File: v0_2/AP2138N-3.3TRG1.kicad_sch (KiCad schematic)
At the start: 9 parts, among them IC3 AP2138N-3.3TRG1, J1 S2B-PH-SM4-TB_LF__SN_, Q1 DMG2301L-7, Q2 DMG2301L-7, Q4 DMN3731U-13

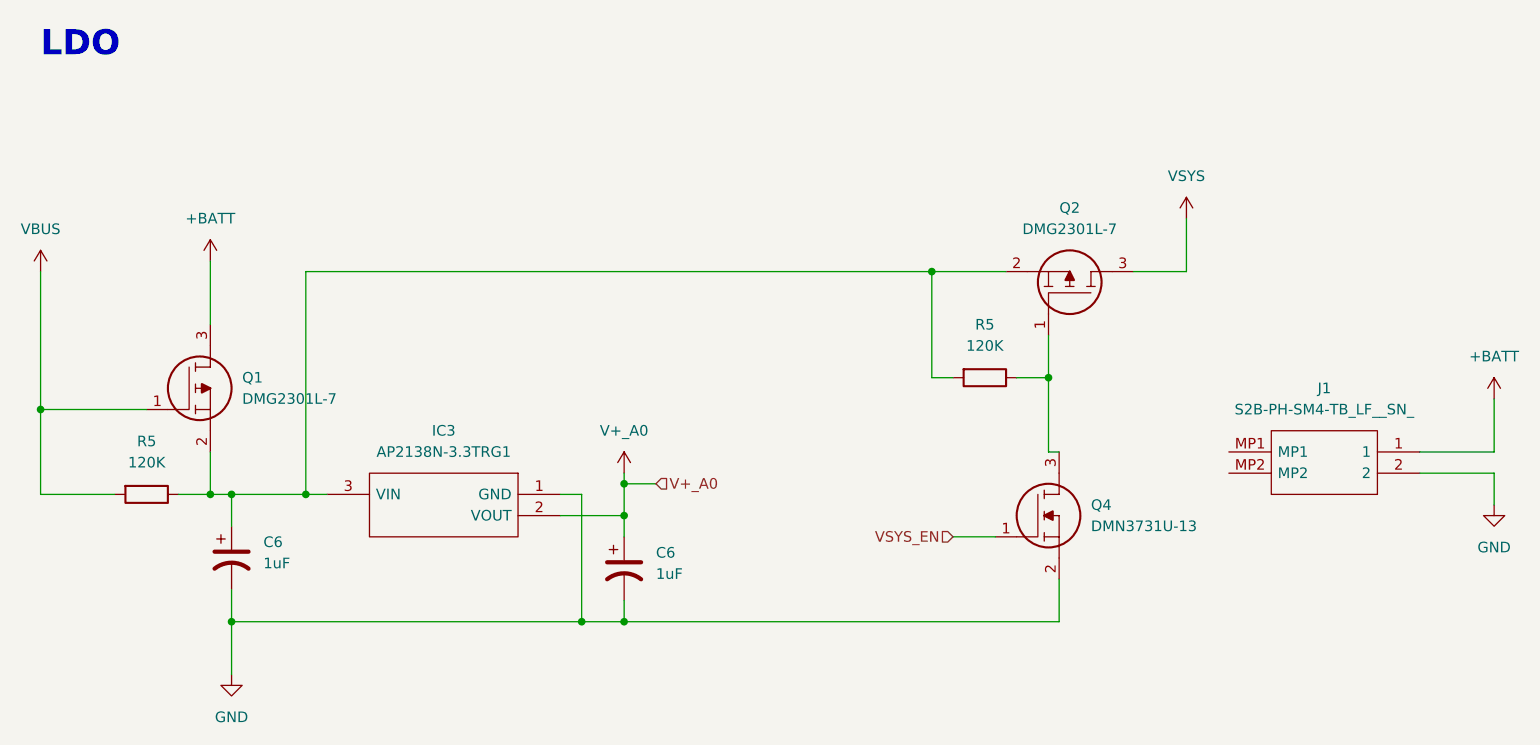
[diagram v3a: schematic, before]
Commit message: rename i2c and add button
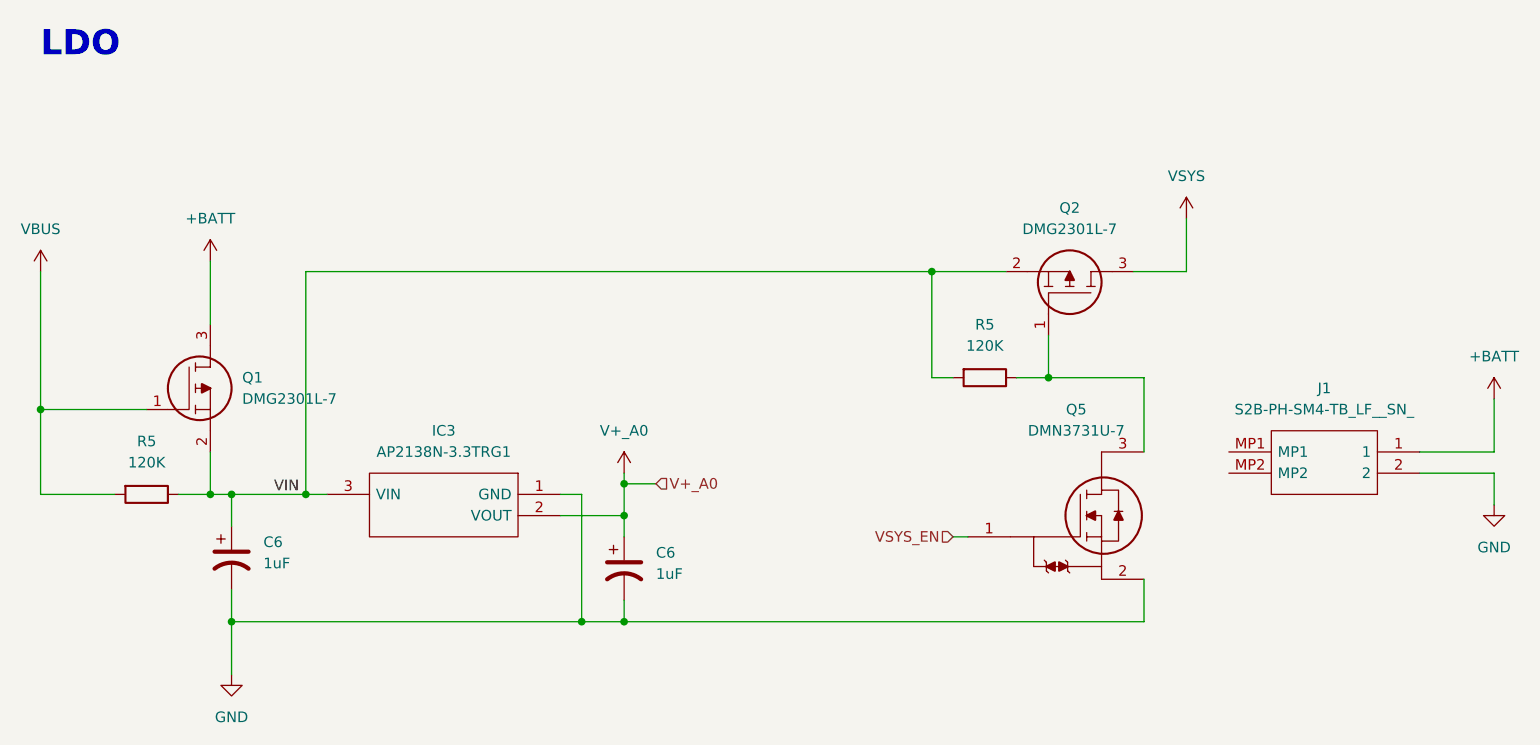
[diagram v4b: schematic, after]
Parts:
- removed Q4: DMN3731U-13, DMN3731U-13:SOT96P240X110-3N, symbol DMN3731U-13:DMN3731U-13
- added Q5: DMN3731U-7, DMN3731U-7:SOT96P240X110-3N, symbol DMN3731U-7:DMN3731U-7
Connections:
- net GND: now also Q5.2
- net VSYS_EN: now also Q5.1
- net at Q2.1, R5.1: now also Q5.3
- net VIN: now reaches C6.1, IC3.3 (VIN), Q1.2, Q2.2, R5.1, R5.2
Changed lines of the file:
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@@
   (junction (at 99.06 90.17) (diameter 0) (color 0 0 0 0)
   )
+  (junction (at 185.42 63.5) (diameter 0) (color 0 0 0 0)
+  )
+  (junction (at 110.49 90.17) (diameter 0) (color 0 0 0 0)
+  )
+  (junction (at 148.59 88.9) (diameter 0) (color 0 0 0 0)
+  )
+  (junction (at 78.74 80.01) (diameter 0) (color 0 0 0 0)
+  )
   (junction (at 199.39 76.2) (diameter 0) (color 0 0 0 0)
   )
-  (junction (at 185.42 63.5) (diameter 0) (color 0 0 0 0)
-  )
-  (junction (at 110.49 90.17) (diameter 0) (color 0 0 0 0)
-  )
-  (junction (at 148.59 88.9) (diameter 0) (color 0 0 0 0)
-  )
-  (junction (at 78.74 80.01) (diameter 0) (color 0 0 0 0)
+  (wire (pts (xy 210.82 76.2) (xy 199.39 76.2))
+    (stroke (width 0) (type default))
   )
   (wire (pts (xy 99.06 62.23) (xy 99.06 69.85))
@@
     (stroke (width 0) (type default))
   )
-  (wire (pts (xy 148.59 105.41) (xy 200.66 105.41))
+  (wire (pts (xy 148.59 105.41) (xy 210.82 105.41))
     (stroke (width 0) (type default))
   )
@@
     (stroke (width 0) (type default))
   )
-  (wire (pts (xy 187.96 95.25) (xy 193.04 95.25))
+  (wire (pts (xy 187.96 95.25) (xy 189.738 95.25))
     (stroke (width 0) (type default))
   )
@@
     (stroke (width 0) (type default))
   )
-  (wire (pts (xy 199.39 85.09) (xy 199.39 76.2))
-    (stroke (width 0) (type default))
-  )
   (wire (pts (xy 148.59 88.9) (xy 152.4 88.9))
     (stroke (width 0) (type default))
@@
     (stroke (width 0) (type default))
   )
+  (wire (pts (xy 210.82 85.09) (xy 210.82 76.2))
+    (stroke (width 0) (type default))
+  )
   (wire (pts (xy 199.39 71.12) (xy 199.39 76.2))
     (stroke (width 0) (type default))
@@
     (stroke (width 0) (type default))
   )
-  (wire (pts (xy 200.66 85.09) (xy 199.39 85.09))
+  (wire (pts (xy 210.82 100.33) (xy 210.82 105.41))
     (stroke (width 0) (type default))
   )
@@
   )
   (wire (pts (xy 101.6 105.41) (xy 101.6 111.76))
-    (stroke (width 0) (type default))
-  )
-  (wire (pts (xy 200.66 100.33) (xy 200.66 105.41))
     (stroke (width 0) (type default))
   )
@@
   (text "LDO" (at 78.74 38.1 0)
     (effects (font (face "Ubuntu") (size 3 3) (thickness 1) bold) (justify left bottom))
+  )
+  (label "VIN" (at 106.68 90.17 0) (fields_autoplaced)
+    (effects (font (size 1.27 1.27)) (justify left bottom))
   )
   (hierarchical_label "VSYS_EN" (shape input) (at 187.96 95.25 180) (fields_autoplaced)
@@
     )
   )
-  (symbol (lib_id "DMN3731U-13:DMN3731U-13") (at 193.04 95.25 0) (unit 1)
-    (in_bom yes) (on_board yes) (dnp no) (fields_autoplaced)
-    (property "Reference" "Q4" (at 204.47 91.44 0)
-      (effects (font (size 1.27 1.27)) (justify left))
-    )
-    (property "Value" "DMN3731U-13" (at 204.47 93.98 0)
-      (effects (font (size 1.27 1.27)) (justify left))
-    )
-    (property "Footprint" "DMN3731U-13:SOT96P240X110-3N" (at 204.47 96.52 0)
-      (effects (font (size 1.27 1.27)) (justify left) hide)
-    )
-    (property "Datasheet" "https://www.diodes.com/assets/Datasheets/DMN3731U.pdf" (at 204.47 99.06 0)
-      (effects (font (size 1.27 1.27)) (justify left) hide)
-    )
-    (property "Description" "MOSFET MOSFET BVDSS: 25V-30V" (at 204.47 101.6 0)
-      (effects (font (size 1.27 1.27)) (justify left) hide)
-    )
-    (property "Height" "1.1" (at 204.47 104.14 0)
-      (effects (font (size 1.27 1.27)) (justify left) hide)
-    )
-    (property "Manufacturer_Name" "Diodes Inc." (at 204.47 106.68 0)
-      (effects (font (size 1.27 1.27)) (justify left) hide)
-    )
-    (property "Manufacturer_Part_Number" "DMN3731U-13" (at 204.47 109.22 0)
-      (effects (font (size 1.27 1.27)) (justify left) hide)
-    )
-    (property "Mouser Part Number" "621-DMN3731U-13" (at 204.47 111.76 0)
-      (effects (font (size 1.27 1.27)) (justify left) hide)
-    )
-    (property "Mouser Price/Stock" "https://www.mouser.co.uk/ProductDetail/Diodes-Incorporated/DMN3731U-13?qs=EBDBlbfErPwOKX9Ga5s0uA%3D%3D" (at 204.47 114.3 0)
-      (effects (font (size 1.27 1.27)) (justify left) hide)
-    )
-    (property "Arrow Part Number" "" (at 204.47 116.84 0)
-      (effects (font (size 1.27 1.27)) (justify left) hide)
-    )
-    (property "Arrow Price/Stock" "" (at 204.47 119.38 0)
-      (effects (font (size 1.27 1.27)) (justify left) hide)
-    )
-    (pin "1")
-    (pin "2")
-    (pin "3")
-    (instances
-      (project "v0_2"
-        (path "/678523e5-508b-4706-b0e0-f17e466a8d09/3580e7c3-86d9-4e19-aad4-f7334a732566"
-          (reference "Q4") (unit 1)
-        )
-      )
-    )
-  )
   (symbol (lib_id "Device:R") (at 91.44 90.17 270) (unit 1)
     (in_bom yes) (on_board yes) (dnp no) (fields_autoplaced)
@@
         )
       )
+    )
+  )
+  (symbol (lib_id "DMN3731U-7:DMN3731U-7") (at 198.12 95.25 0) (unit 1)
+    (in_bom yes) (on_board yes) (dnp no) (fields_autoplaced)
+    (property "Reference" "Q5" (at 202.7174 80.01 0)
+      (effects (font (size 1.27 1.27)))
+    )
+    (property "Value" "DMN3731U-7" (at 202.7174 82.55 0)
+      (effects (font (size 1.27 1.27)))
+    )
+    (property "Footprint" "DMN3731U-7:SOT96P240X110-3N" (at 212.852 76.2 0)
+      (effects (font (size 1.27 1.27)) (justify left) hide)
+    )
+    (property "Datasheet" "https://www.mouser.fr/datasheet/2/115/DMN3731U-1594715.pdf" (at 212.852 78.74 0)
+      (effects (font (size 1.27 1.27)) (justify left) hide)
+    )
+    (property "Description" "MOSFET MOSFET BVDSS: 25V-30V" (at 212.852 81.28 0)
+      (effects (font (size 1.27 1.27)) (justify left) hide)
+    )
+    (property "Height" "1.1" (at 212.852 83.82 0)
+      (effects (font (size 1.27 1.27)) (justify left) hide)
+    )
+    (property "Manufacturer_Name" "Diodes Inc." (at 212.852 86.36 0)
+      (effects (font (size 1.27 1.27)) (justify left) hide)
+    )
+    (property "Manufacturer_Part_Number" "DMN3731U-7" (at 212.852 88.9 0)
+      (effects (font (size 1.27 1.27)) (justify left) hide)
+    )
+    (property "Mouser Part Number" "621-DMN3731U-7" (at 212.852 91.44 0)
+      (effects (font (size 1.27 1.27)) (justify left) hide)
+    )
+    (property "Mouser Price/Stock" "https://www.mouser.co.uk/ProductDetail/Diodes-Incorporated/DMN3731U-7?qs=EBDBlbfErPyEqvOCBrONHQ%3D%3D" (at 212.852 93.98 0)
+      (effects (font (size 1.27 1.27)) (justify left) hide)
+    )
+    (property "Arrow Part Number" "" (at 212.852 96.52 0)
+      (effects (font (size 1.27 1.27)) (justify left) hide)
+    )
+    (property "Arrow Price/Stock" "" (at 212.852 99.06 0)
+      (effects (font (size 1.27 1.27)) (justify left) hide)
+    )
+    (pin "1")
+    (pin "2")
+    (pin "3")
+    (instances
+      (project "v0_2"
+        (path "/678523e5-508b-4706-b0e0-f17e466a8d09/3580e7c3-86d9-4e19-aad4-f7334a732566"
+          (reference "Q5") (unit 1)
+        )
+      )

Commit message: power line
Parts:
- added J6: Conn_01x02_Pin, Connector_PinHeader_1.27mm:PinHeader_1x02_P1.27mm_Vertical, symbol Connector:Conn_01x02_Pin
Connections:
- net +BATT: now also J6.1 (Pin_1)
- net GND: now also J6.2 (Pin_2)
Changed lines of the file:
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@@
   (junction (at 101.6 105.41) (diameter 0) (color 0 0 0 0)
   )
+  (junction (at 247.65 85.09) (diameter 0) (color 0 0 0 0)
+  )
   (junction (at 148.59 105.41) (diameter 0) (color 0 0 0 0)
   )
@@
   (junction (at 199.39 76.2) (diameter 0) (color 0 0 0 0)
   )
+  (junction (at 250.19 87.63) (diameter 0) (color 0 0 0 0)
+  )
   (wire (pts (xy 210.82 76.2) (xy 199.39 76.2))
     (stroke (width 0) (type default))
@@
     (stroke (width 0) (type default))
   )
+  (wire (pts (xy 243.84 99.06) (xy 250.19 99.06))
+    (stroke (width 0) (type default))
+  )
   (wire (pts (xy 78.74 80.01) (xy 78.74 90.17))
     (stroke (width 0) (type default))
@@
     (stroke (width 0) (type default))
   )
-  (wire (pts (xy 243.84 85.09) (xy 252.73 85.09))
+  (wire (pts (xy 243.84 85.09) (xy 247.65 85.09))
     (stroke (width 0) (type default))
   )
@@
     (stroke (width 0) (type default))
   )
-  (wire (pts (xy 243.84 87.63) (xy 252.73 87.63))
+  (wire (pts (xy 243.84 87.63) (xy 250.19 87.63))
     (stroke (width 0) (type default))
   )
@@
     (stroke (width 0) (type default))
   )
-  (wire (pts (xy 187.96 95.25) (xy 189.738 95.25))
+  (wire (pts (xy 184.15 95.25) (xy 189.738 95.25))
     (stroke (width 0) (type default))
   )
@@
     (stroke (width 0) (type default))
   )
+  (wire (pts (xy 247.65 85.09) (xy 252.73 85.09))
+    (stroke (width 0) (type default))
+  )
   (wire (pts (xy 185.42 76.2) (xy 185.42 63.5))
     (stroke (width 0) (type default))
   )
+  (wire (pts (xy 250.19 87.63) (xy 252.73 87.63))
+    (stroke (width 0) (type default))
+  )
   (wire (pts (xy 99.06 85.09) (xy 99.06 90.17))
     (stroke (width 0) (type default))
@@
     (stroke (width 0) (type default))
   )
+  (wire (pts (xy 250.19 99.06) (xy 250.19 87.63))
+    (stroke (width 0) (type default))
+  )
+  (wire (pts (xy 247.65 96.52) (xy 247.65 85.09))
+    (stroke (width 0) (type default))
+  )
   (wire (pts (xy 101.6 90.17) (xy 110.49 90.17))
     (stroke (width 0) (type default))
@@
   )
   (wire (pts (xy 101.6 105.41) (xy 101.6 111.76))
+    (stroke (width 0) (type default))
+  )
+  (wire (pts (xy 243.84 96.52) (xy 247.65 96.52))
     (stroke (width 0) (type default))
   )
@@
     (effects (font (size 1.27 1.27)) (justify left bottom))
   )
-  (hierarchical_label "VSYS_EN" (shape input) (at 187.96 95.25 180) (fields_autoplaced)
+  (hierarchical_label "VSYS_EN" (shape input) (at 184.15 95.25 180) (fields_autoplaced)
     (effects (font (size 1.27 1.27)) (justify right))
   )
@@
         )
       )
+    )
+  )
+  (symbol (lib_id "Connector:Conn_01x02_Pin") (at 238.76 96.52 0) (unit 1)
+    (in_bom yes) (on_board yes) (dnp no) (fields_autoplaced)
+    (property "Reference" "J6" (at 239.395 91.44 0)
+      (effects (font (size 1.27 1.27)))
+    )
+    (property "Value" "Conn_01x02_Pin" (at 239.395 93.98 0)
+      (effects (font (size 1.27 1.27)))
+    )
+    (property "Footprint" "Connector_PinHeader_1.27mm:PinHeader_1x02_P1.27mm_Vertical" (at 238.76 96.52 0)
+      (effects (font (size 1.27 1.27)) hide)
+    )
+    (property "Datasheet" "~" (at 238.76 96.52 0)
+      (effects (font (size 1.27 1.27)) hide)
+    )
+    (pin "1")
+    (pin "2")
+    (instances
+      (project "v0_2"
+        (path "/678523e5-508b-4706-b0e0-f17e466a8d09/3580e7c3-86d9-4e19-aad4-f7334a732566"
+          (reference "J6") (unit 1)
+        )
+      )
